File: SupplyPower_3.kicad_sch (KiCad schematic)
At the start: 3 parts, among them U1 R-78E3.3-1.0

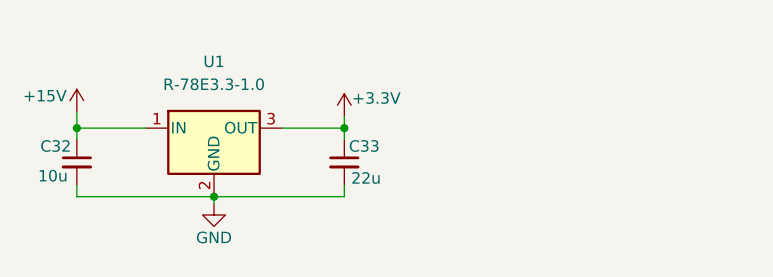
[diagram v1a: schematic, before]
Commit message: Изменил схему
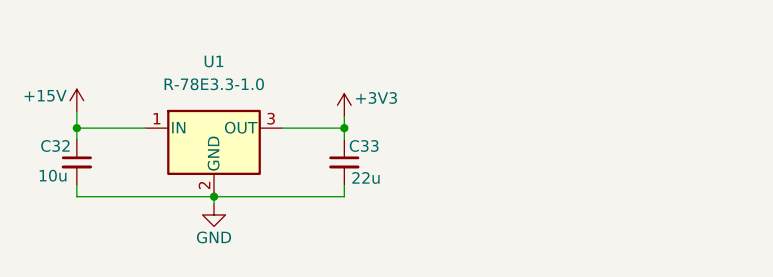
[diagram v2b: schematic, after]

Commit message: Убрал питание 3.3В
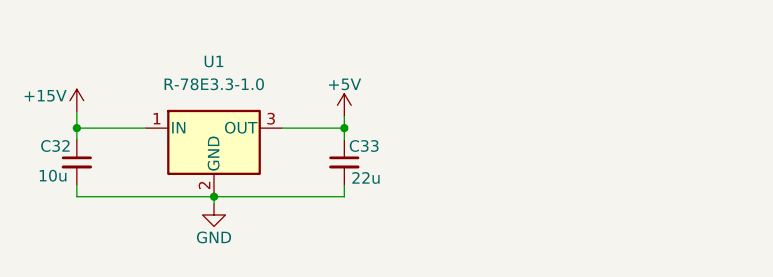
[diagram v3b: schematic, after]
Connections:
- net +3V3 renamed +5V
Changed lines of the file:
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@@
 	)
 	(symbol
-		(lib_id "power:+3.3V")
+		(lib_id "power:+5V")
 		(at 189.992 94.742 0)
 		(unit 1)
@@
 		(on_board yes)
 		(dnp no)
-		(property "Reference" "#PWR0149"
+		(property "Reference" "#PWR149"
 			(at 189.992 98.552 0)
 			(effects
@@
 			)
 		)
-		(property "Value" "+3V3"
-			(at 193.548 92.71 0)
+		(property "Value" "+5V"
+			(at 189.992 91.186 0)
 			(effects
 				(font
@@
 			)
 		)
-		(property "Description" ""
+		(property "Description" "Power symbol creates a global label with name \"+5V\""
 			(at 189.992 94.742 0)
 			(effects
@@
 			(project "Adapter"
 				(path "/e63e39d7-6ac0-4ffd-8aa3-1841a4541b55/48506f31-24d2-459a-84b5-2cde043f3b1b"
-					(reference "#PWR0149")
+					(reference "#PWR149")
 					(unit 1)
 				)

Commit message: Развел стойку фазы А
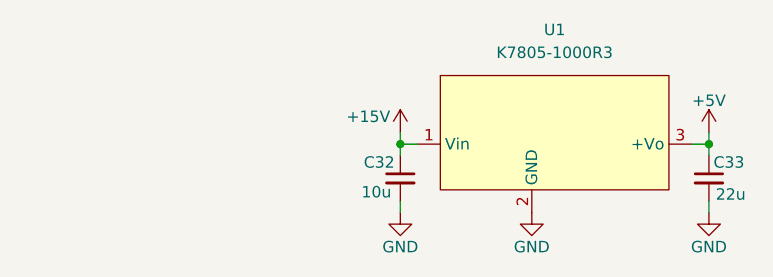
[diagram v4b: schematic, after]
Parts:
- removed U1: R-78E3.3-1.0, Converter_DCDC:Converter_DCDC_RECOM_R-78E-0.5_THT, symbol Regulator_Switching:R-78E3.3-1.0
- added U1: K7805-1000R3, K78xx-1000R3, symbol DCDC_My:K78xx-1000R3
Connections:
- net +15V: now also U1.1 (Vin)
- net +5V: now also U1.3 (+Vo)
- net GND: now also U1.2 (GND)
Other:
- moved on the sheet: C32, C33
